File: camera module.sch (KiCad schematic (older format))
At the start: 152 parts, among them J1 Conn_01x02, J10 Conn_01x04, J11 Conn_01x05, J12 Conn_01x06, J13 Conn_01x02, J15 Conn_02x30_Odd_Even, J17 USB_B_Micro, J18 Conn_01x03, J2 USB_OTG, J3 Conn_01x15, J4 Conn_02x15_Counter_Clockwise, J5 HDMI, J6 Conn_01x15, J7 Conn_01x02, J8 HDMI, J9 HDMI, Q1 EM6K34T2CR, Q10 DMG2305UX, Q11 DMMT5401-7-F, Q12 DMG2305UX, Q2 Q_NMOS_GSD, Q3 Q_NMOS_GSD, Q4 Q_NMOS_GSD, Q5 Q_NMOS_GSD, Q6 Q_NMOS_GSD, Q7 DMMT5401-7-F, Q8 DMG2305UX, Q9 DMMT5401-7-F, SW1 SW_SPST, U1 TPS563208, U10 FSUSB42UMX, U11 USB_A, U2 PAM2306AYPKE, U3 LTC3406ES5-1.2, U4 TS3DDR3812RUAR, U5 TLV70228_SOT23-5, U6 XC6222B181MR-G, U7 LSM6DS3, U8 HDMIULC6-4SC6, U9 AP2331W, Y1 SIT8008AI-73-XXS-33.333333E

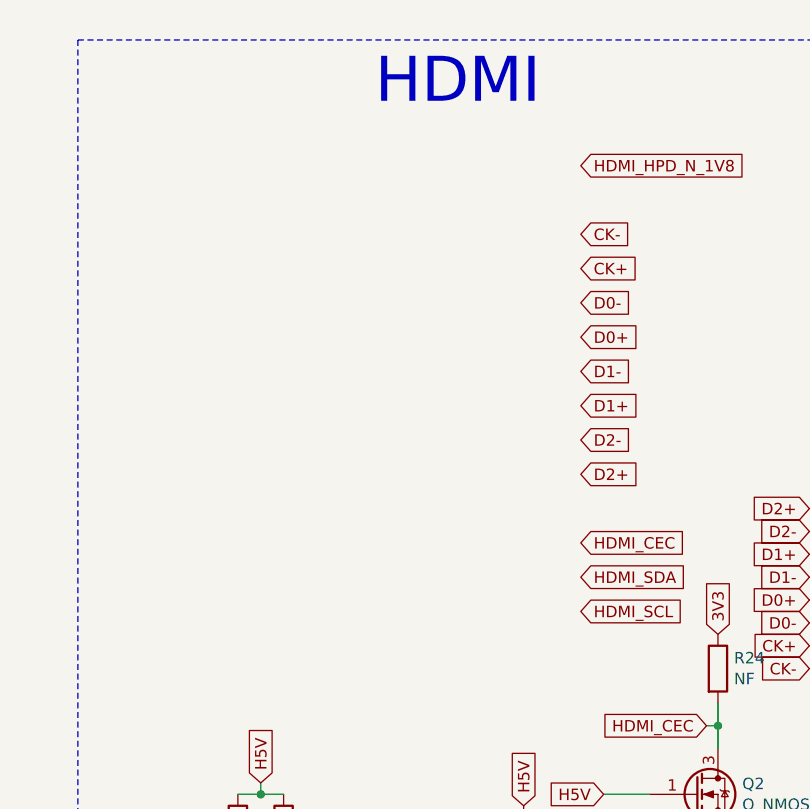
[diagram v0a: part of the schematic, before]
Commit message: Joe crashed KiCAD, not my fault
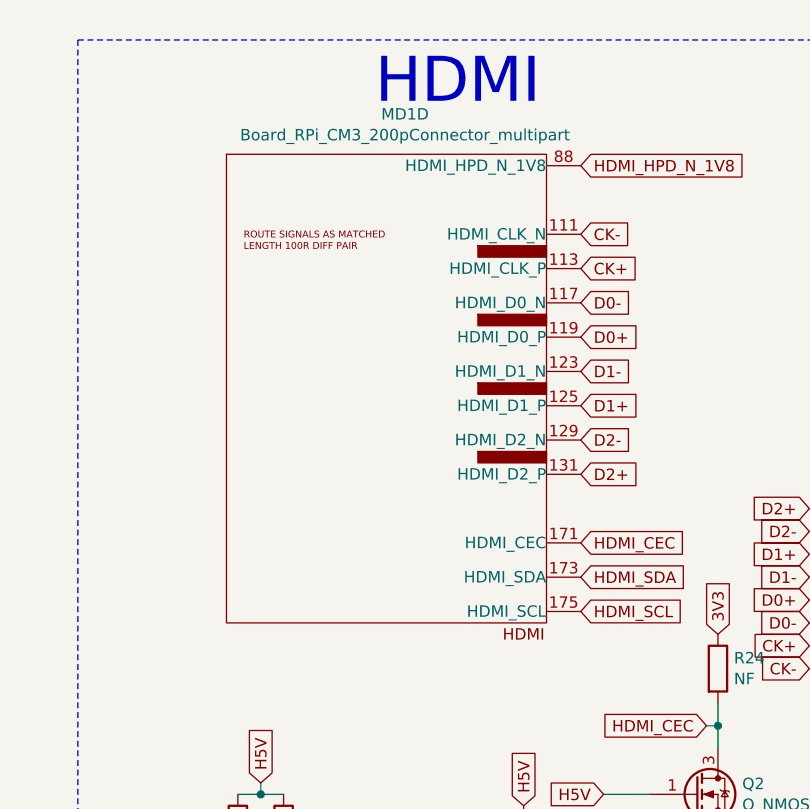
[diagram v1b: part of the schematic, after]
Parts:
- added unit 4 of MD1
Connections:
- net CK+: now also MD1.113 (HDMI_CLK_P)
- net CK-: now also MD1.111 (HDMI_CLK_N)
- net D0+: now also MD1.119 (HDMI_D0_P)
- net D0-: now also MD1.117 (HDMI_D0_N)
- net D1+: now also MD1.125 (HDMI_D1_P)
- net D1-: now also MD1.123 (HDMI_D1_N)
- net D2+: now also MD1.131 (HDMI_D2_P)
- net D2-: now also MD1.129 (HDMI_D2_N)
- net HDMI_CEC: now also MD1.171 (HDMI_CEC)
- net HDMI_HPD_N_1V8: now also MD1.88 (HDMI_HPD_N_1V8)
- net HDMI_SCL: now also MD1.175 (HDMI_SCL)
- net HDMI_SDA: now also MD1.173 (HDMI_SDA)
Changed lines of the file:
@@
 EESchema Schematic File Version 4
-LIBS:camera module-cache
 EELAYER 26 0
 EELAYER END
@@
 NoConn ~ 19200 5150
 NoConn ~ 19200 5300
+$Comp
+L KiCADinfo_RPi-modules:Board_RPi_CM3_200pConnector_multipart MD1
+U 4 1 5C790B9B
+P 12100 2200
+F 0 "MD1" H 12181 3475 50  0000 C CNN
+F 1 "Board_RPi_CM3_200pConnector_multipart" H 12181 3384 50  0000 C CNN
+F 2 "_" H 18075 -650 10  0001 C CNN
+F 3 "_" H 18075 -650 10  0001 C CNN
+F 4 "_" H 18075 -650 10  0001 C CNN "Manf#"
+F 5 "_" H 18075 -650 10  0001 C CNN "Manf"
+F 6 "_" H 18075 -650 10  0001 C CNN "Optn"
+	4    12100 2200
+	1    0    0    -1
+$EndComp
 $EndSCHEMATC

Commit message: Tweaks to routing, 4th mounting hole added, DRC issues fixed
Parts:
- added H1, H2, H3, H4: MountingHole, MountingHole:MountingHole_2.2mm_M2_DIN965_Pad, symbol Mechanical:MountingHole
- MD1: footprint _ -> 1473149-4:TE_1473149-4
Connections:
- net CAM0_onboard_CK is gone; now on net CAM0_onboard_CLK: U4.37 (C2)
- net CAM0_CLK renamed CAM0_onboard_CLK
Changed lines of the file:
@@
 EESchema Schematic File Version 4
+LIBS:camera module-cache
 EELAYER 26 0
 EELAYER END
@@
 NoConn ~ 8300 3500
 Text GLabel 8950 3100 2    50   Input ~ 0
-CAM0_CLK
+CAM0_onboard_CLK
 Wire Wire Line
 	8950 2900 8800 2900
@@
 $EndComp
 Text GLabel 9250 4550 2    50   Input ~ 0
-CAM0_CLK
+CAM0_onboard_CLK
 Wire Wire Line
 	8950 4550 8850 4550
@@
 CAM0_onboard_DN1
 Text GLabel 6400 7750 2    50   Input ~ 0
-CAM0_onboard_CK
+CAM0_onboard_CLK
 Text GLabel 6400 7850 2    50   Input ~ 0
 CAM0_onboard_IO0
@@
 F 0 "MD1" H 12181 3475 50  0000 C CNN
 F 1 "Board_RPi_CM3_200pConnector_multipart" H 12181 3384 50  0000 C CNN
-F 2 "_" H 18075 -650 10  0001 C CNN
+F 2 "1473149-4:TE_1473149-4" H 18075 -650 10  0001 C CNN
 F 3 "_" H 18075 -650 10  0001 C CNN
 F 4 "_" H 18075 -650 10  0001 C CNN "Manf#"
@@
 	1    0    0    -1
 $EndComp
+$Comp
+L Mechanical:MountingHole H1
+U 1 1 5C735C14
+P 19600 13450
+F 0 "H1" H 19700 13496 50  0000 L CNN
+F 1 "MountingHole" H 19700 13405 50  0000 L CNN
+F 2 "MountingHole:MountingHole_2.2mm_M2_DIN965_Pad" H 19600 13450 50  0001 C CNN
+F 3 "~" H 19600 13450 50  0001 C CNN
+	1    19600 13450
+	1    0    0    -1
+$EndComp
+$Comp
+L Mechanical:MountingHole H2
+U 1 1 5C7360BE
+P 19800 13450
+F 0 "H2" H 19900 13496 50  0000 L CNN
+F 1 "MountingHole" H 19900 13405 50  0000 L CNN
+F 2 "MountingHole:MountingHole_2.2mm_M2_DIN965_Pad" H 19800 13450 50  0001 C CNN
+F 3 "~" H 19800 13450 50  0001 C CNN
+	1    19800 13450
+	1    0    0    -1
+$EndComp
+$Comp
+L Mechanical:MountingHole H3
+U 1 1 5C736218
+P 20050 13450
+F 0 "H3" H 20150 13496 50  0000 L CNN
+F 1 "MountingHole" H 20150 13405 50  0000 L CNN
+F 2 "MountingHole:MountingHole_2.2mm_M2_DIN965_Pad" H 20050 13450 50  0001 C CNN
+F 3 "~" H 20050 13450 50  0001 C CNN
+	1    20050 13450
+	1    0    0    -1
+$EndComp
+$Comp
+L Mechanical:MountingHole H4
+U 1 1 5C73901E
+P 20250 13450
+F 0 "H4" H 20350 13496 50  0000 L CNN
+F 1 "MountingHole" H 20350 13405 50  0000 L CNN
+F 2 "MountingHole:MountingHole_2.2mm_M2_DIN965_Pad" H 20250 13450 50  0001 C CNN
+F 3 "~" H 20250 13450 50  0001 C CNN
+	1    20250 13450
+	1    0    0    -1
+$EndComp

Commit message: Final files. As sent to manufacture
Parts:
- C10, C11, C15, C16, C17, C18, C19, C6, C7: value C -> 100n
- C31: value C -> 22u
- C32: value C -> 100nf
- C33: value C -> 47u
- D10, D11, D12, D14, D15, D16, D3, D4, D5, D7, D8, D9: footprint LED_SMD:LED_2512_6332Metric_Pad1.52x3.35mm_HandSolder -> LED_SMD:LED_0805_2012Metric_Pad1.15x1.40mm_HandSolder
- L1, L12, L3, L5: footprint Inductor_SMD:L_0805_2012Metric_Pad1.15x1.40mm_HandSolder -> Inductor_SMD:L_0603_1608Metric_Pad1.05x0.95mm_HandSolder
- L6: value L -> 3.3u; footprint Inductor_SMD:L_0805_2012Metric -> Inductor_SMD_local:SDR0805-3R3ML-footprint
- R11, R13, R52, R55, R56, R58, R7: value R -> 10k
- R53, R57, R59: value R -> 47k
- R54: value R -> 56.2k
